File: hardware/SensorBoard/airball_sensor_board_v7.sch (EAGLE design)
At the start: 27 parts, among them J1 FEMALE 2x3

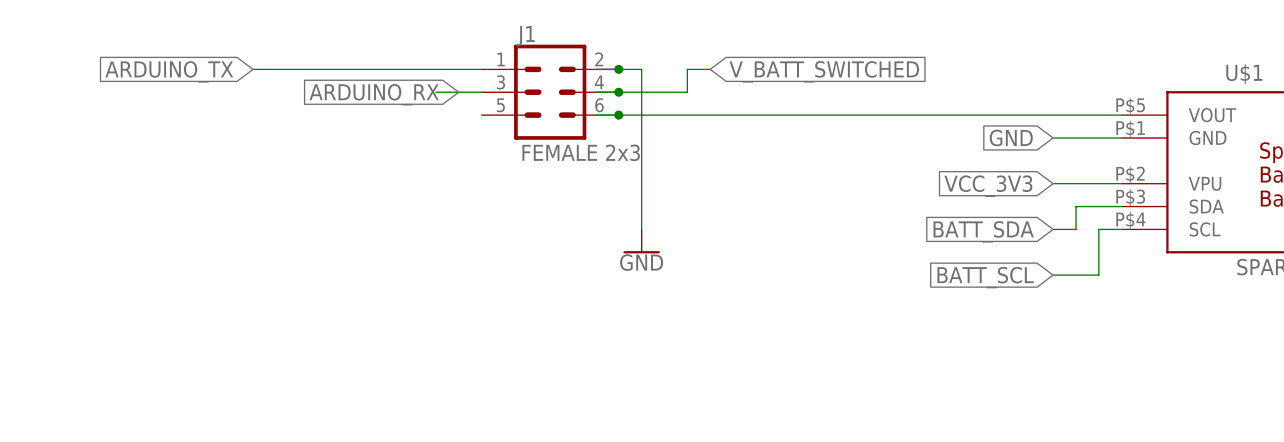
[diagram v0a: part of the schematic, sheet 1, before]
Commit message: Minor fix to remove an airwire.
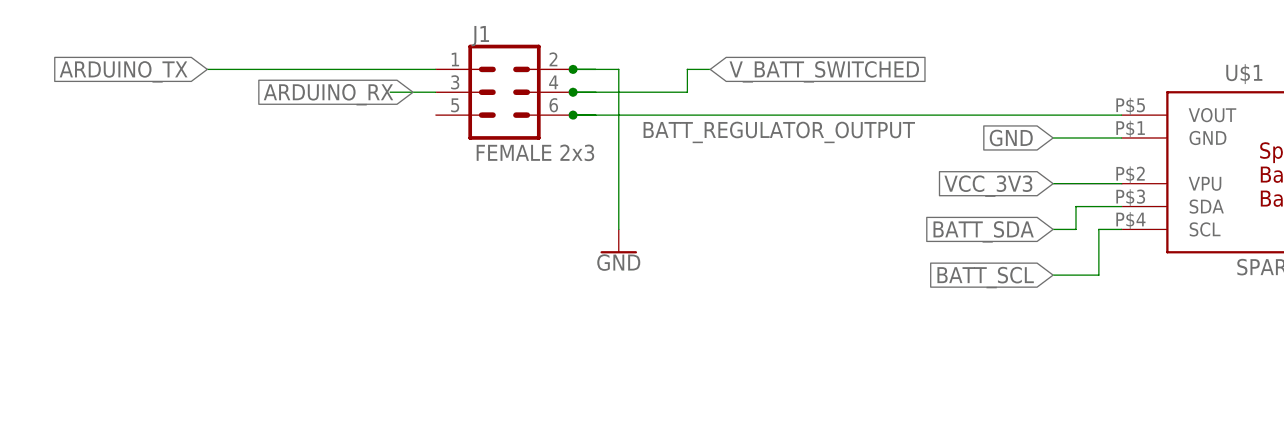
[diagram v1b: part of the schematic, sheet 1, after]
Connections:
- net N$1 renamed BATT_REGULATOR_OUTPUT
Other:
- moved on the sheet: J1
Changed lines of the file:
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@@
 <attribute name="VALUE" x="152.4" y="119.38" size="1.778" layer="96"/>
 </instance>
-<instance part="GND3" gate="1" x="86.36" y="121.92" smashed="yes">
-<attribute name="VALUE" x="86.36" y="121.666" size="1.778" layer="96" align="top-center"/>
+<instance part="GND3" gate="1" x="83.82" y="121.92" smashed="yes">
+<attribute name="VALUE" x="83.82" y="121.666" size="1.778" layer="96" align="top-center"/>
 </instance>
-<instance part="J1" gate="G$1" x="76.2" y="139.7" smashed="yes">
-<attribute name="NAME" x="72.644" y="145.288" size="1.778" layer="95" font="vector"/>
-<attribute name="VALUE" x="72.898" y="133.858" size="1.778" layer="96" font="vector" align="top-left"/>
+<instance part="J1" gate="G$1" x="71.12" y="139.7" smashed="yes">
+<attribute name="NAME" x="67.564" y="145.288" size="1.778" layer="95" font="vector"/>
+<attribute name="VALUE" x="67.818" y="133.858" size="1.778" layer="96" font="vector" align="top-left"/>
 </instance>
 </instances>
@@
 <segment>
 <pinref part="GND3" gate="1" pin="GND"/>
-<wire x1="81.28" y1="142.24" x2="83.82" y2="142.24" width="0.1524" layer="91"/>
-<wire x1="83.82" y1="142.24" x2="86.36" y2="142.24" width="0.1524" layer="91"/>
-<wire x1="86.36" y1="142.24" x2="86.36" y2="124.46" width="0.1524" layer="91"/>
+<wire x1="81.28" y1="142.24" x2="78.74" y2="142.24" width="0.1524" layer="91"/>
+<wire x1="78.74" y1="142.24" x2="83.82" y2="142.24" width="0.1524" layer="91"/>
+<wire x1="83.82" y1="142.24" x2="83.82" y2="124.46" width="0.1524" layer="91"/>
 <pinref part="J1" gate="G$1" pin="2"/>
-<junction x="83.82" y="142.24"/>
+<junction x="78.74" y="142.24"/>
 </segment>
 </net>
@@
 </segment>
 </net>
-<net name="N$1" class="0">
+<net name="BATT_REGULATOR_OUTPUT" class="0">
 <segment>
 <pinref part="U$1" gate="G$1" pin="VOUT"/>
-<wire x1="139.7" y1="137.16" x2="83.82" y2="137.16" width="0.1524" layer="91"/>
+<wire x1="139.7" y1="137.16" x2="78.74" y2="137.16" width="0.1524" layer="91"/>
 <pinref part="J1" gate="G$1" pin="6"/>
-<wire x1="83.82" y1="137.16" x2="81.28" y2="137.16" width="0.1524" layer="91"/>
-<junction x="83.82" y="137.16"/>
+<wire x1="78.74" y1="137.16" x2="81.28" y2="137.16" width="0.1524" layer="91"/>
+<junction x="78.74" y="137.16"/>
+<label x="86.36" y="134.62" size="1.778" layer="95"/>
 </segment>
 </net>
 <net name="V_BATT_SWITCHED" class="0">
 <segment>
-<wire x1="81.28" y1="139.7" x2="83.82" y2="139.7" width="0.1524" layer="91"/>
-<wire x1="83.82" y1="139.7" x2="91.44" y2="139.7" width="0.1524" layer="91"/>
+<wire x1="81.28" y1="139.7" x2="78.74" y2="139.7" width="0.1524" layer="91"/>
+<wire x1="78.74" y1="139.7" x2="91.44" y2="139.7" width="0.1524" layer="91"/>
 <wire x1="91.44" y1="139.7" x2="91.44" y2="142.24" width="0.1524" layer="91"/>
 <wire x1="91.44" y1="142.24" x2="93.98" y2="142.24" width="0.1524" layer="91"/>
 <label x="93.98" y="142.24" size="1.778" layer="95" xref="yes"/>
 <pinref part="J1" gate="G$1" pin="4"/>
-<junction x="83.82" y="139.7"/>
+<junction x="78.74" y="139.7"/>
 </segment>
 </net>
@@
 <segment>
 <pinref part="J1" gate="G$1" pin="3"/>
-<wire x1="68.58" y1="139.7" x2="63.5" y2="139.7" width="0.1524" layer="91"/>
-<label x="66.04" y="139.7" size="1.778" layer="95" rot="MR0" xref="yes"/>
+<wire x1="63.5" y1="139.7" x2="58.42" y2="139.7" width="0.1524" layer="91"/>
+<label x="60.96" y="139.7" size="1.778" layer="95" rot="MR0" xref="yes"/>
 </segment>
 </net>
@@
 <segment>
 <pinref part="J1" gate="G$1" pin="1"/>
-<wire x1="68.58" y1="142.24" x2="43.18" y2="142.24" width="0.1524" layer="91"/>
-<label x="43.18" y="142.24" size="1.778" layer="95" rot="MR0" xref="yes"/>
+<wire x1="63.5" y1="142.24" x2="38.1" y2="142.24" width="0.1524" layer="91"/>
+<label x="38.1" y="142.24" size="1.778" layer="95" rot="MR0" xref="yes"/>
 </segment>
 </net>

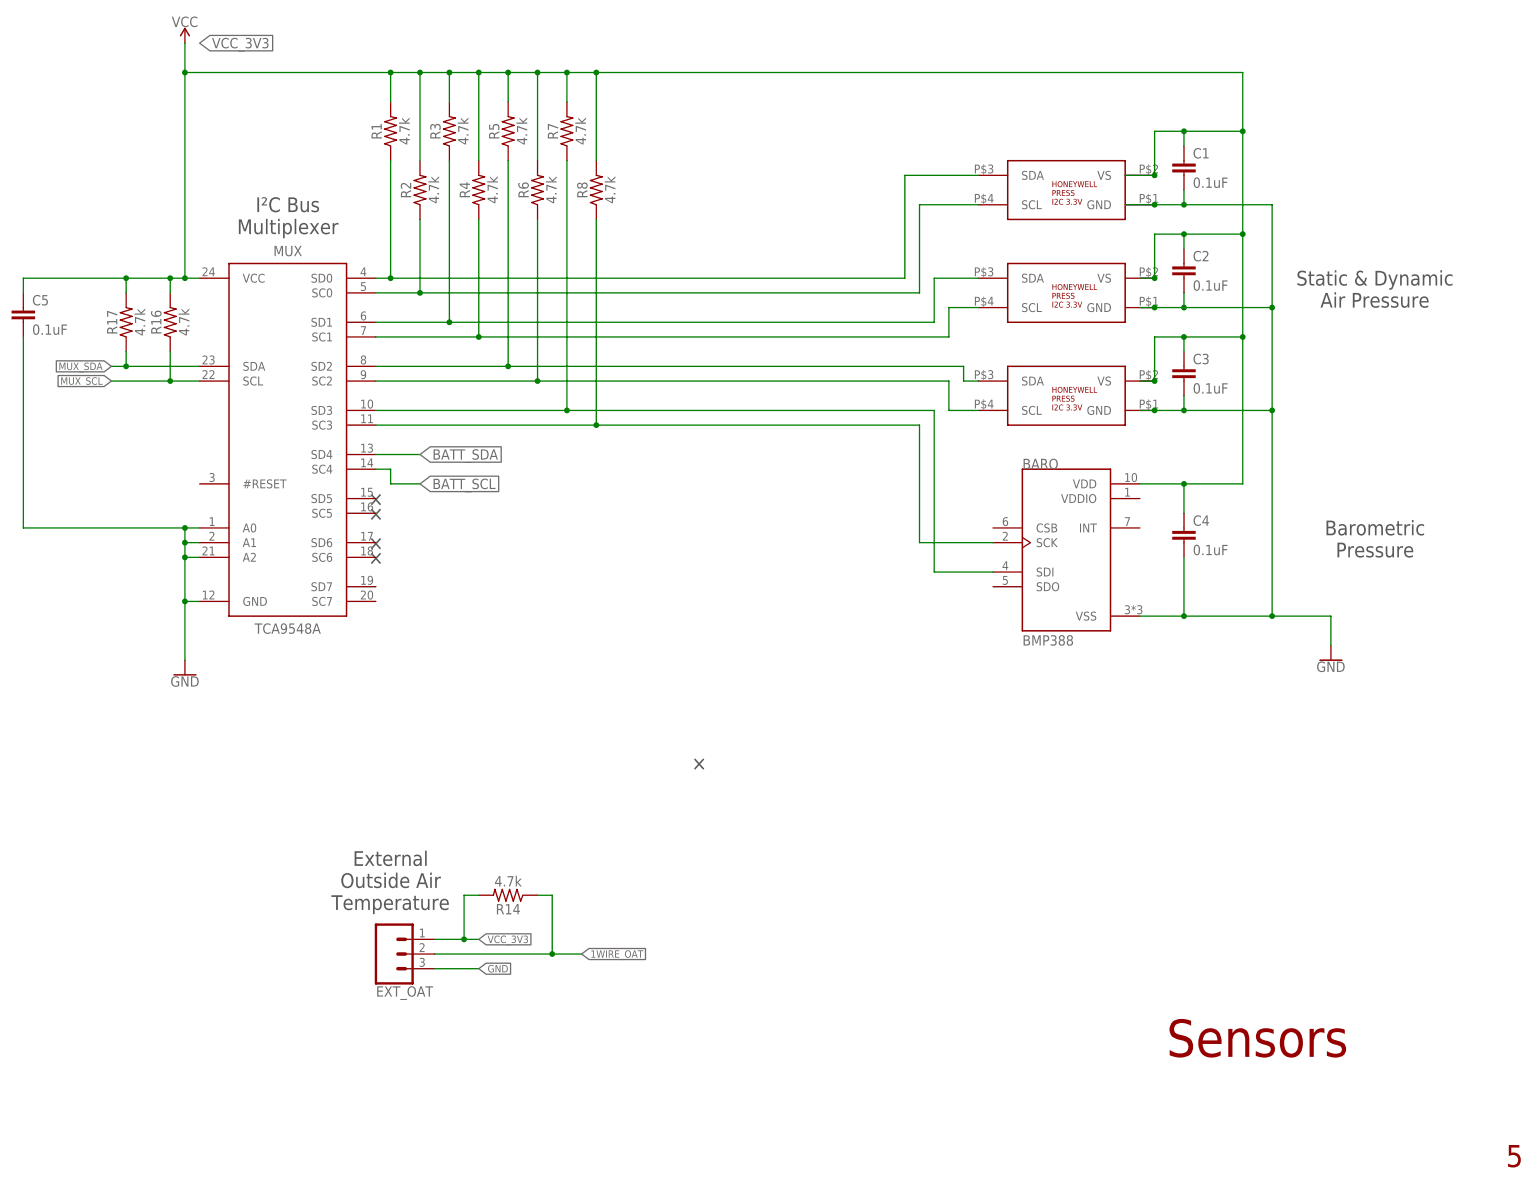
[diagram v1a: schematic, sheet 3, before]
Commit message: Changed use of Bosch BMP388 sensor so that we are using the Adafruit breakout board instead of soldering the sensor on directly. This saves us some finicky SMT work.
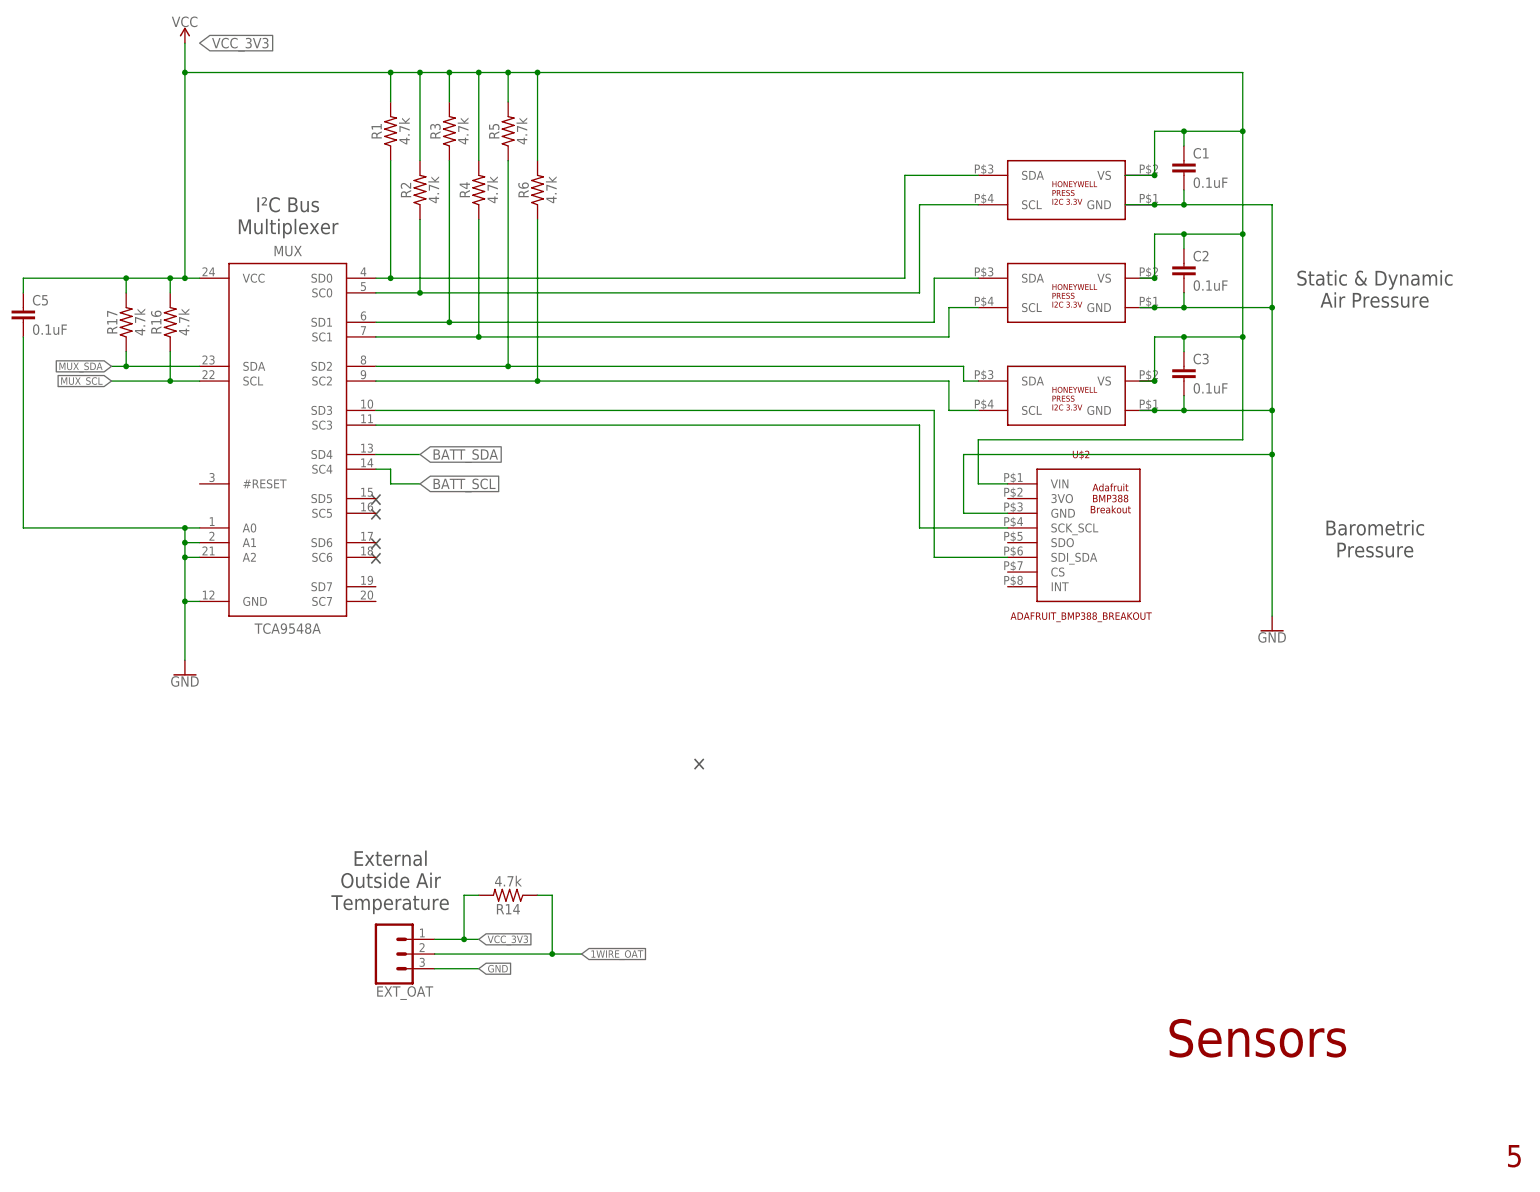
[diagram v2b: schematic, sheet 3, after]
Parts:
- removed BARO: BMP388, BMP388:BMP388
- removed C4: 0.1uF, SparkFun-Capacitors:0.1UF-0603-25V-5%
- removed R7, R8: 4.7k, SparkFun-Resistors:4.7KOHM-0603-1/10W-1%
- added U$2: ADAFRUIT_BMP388_BREAKOUT, airball:ADAFRUIT_BMP388_BREAKOUT
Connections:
- net GND: now also U$2.GND; no longer BARO.VSS, C4.2
- net SCL_BMP_BARO: now also U$2.SCK_SCL; no longer BARO.SCK, R8.1
- net SDA_BMP_BARO: now also U$2.SDI_SDA; no longer BARO.SDI, R7.1
- net VCC_3V3: now also U$2.VIN; no longer BARO.VDD, C4.1, R7.2, R8.2
